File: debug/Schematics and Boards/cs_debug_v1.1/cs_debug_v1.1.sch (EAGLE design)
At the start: 217 parts, among them J1 J-JTAG-CORTEX_SMD, J19 Solar, J3 HIROSE-DF40_50-PIN_CONNECTORS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, J5 J-WURTH-USBC, Q10 2N7002P, Q3 FDN340P, Q4 2N7002P, Q5 FDN340P, Q6 2N7002P, Q7 FDN340P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

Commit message: DBG: change a few passive components for lower cost option.
Have NOT regenerated the BOM or CAM yet
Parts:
- R22, R23, R31, R32, R38, R39, R58: MPN ERJ-3BQF5R1V -> ERJ-U03F5R10V; PART_NO ERJ-3BQF5R1V -> ERJ-U03F5R10V
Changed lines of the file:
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@@
 </part>
 <part name="R58" library="Resistors" deviceset="R-" device="0603" value="5.1">
-<attribute name="MPN" value="ERJ-3BQF5R1V"/>
-<attribute name="PART_NO" value="ERJ-3BQF5R1V"/>
+<attribute name="MPN" value="ERJ-U03F5R10V"/>
+<attribute name="PART_NO" value="ERJ-U03F5R10V"/>
 <attribute name="TOL" value="1%"/>
 </part>
@@
 </part>
 <part name="R38" library="Resistors" deviceset="R-" device="0603" value="5.1">
-<attribute name="MPN" value="ERJ-3BQF5R1V"/>
-<attribute name="PART_NO" value="ERJ-3BQF5R1V"/>
+<attribute name="MPN" value="ERJ-U03F5R10V"/>
+<attribute name="PART_NO" value="ERJ-U03F5R10V"/>
 <attribute name="TOL" value="1%"/>
 </part>
@@
 <part name="U$29" library="SparkFun-PowerSymbols" deviceset="AGND" device=""/>
 <part name="R39" library="Resistors" deviceset="R-" device="0603" value="5.1">
-<attribute name="MPN" value="ERJ-3BQF5R1V"/>
-<attribute name="PART_NO" value="ERJ-3BQF5R1V"/>
+<attribute name="MPN" value="ERJ-U03F5R10V"/>
+<attribute name="PART_NO" value="ERJ-U03F5R10V"/>
 <attribute name="TOL" value="1%"/>
 </part>
@@
 </part>
 <part name="R31" library="Resistors" deviceset="R-" device="0603" value="5.1">
-<attribute name="MPN" value="ERJ-3BQF5R1V"/>
-<attribute name="PART_NO" value="ERJ-3BQF5R1V"/>
+<attribute name="MPN" value="ERJ-U03F5R10V"/>
+<attribute name="PART_NO" value="ERJ-U03F5R10V"/>
 <attribute name="TOL" value="1%"/>
 </part>
@@
 <part name="U$24" library="SparkFun-PowerSymbols" deviceset="AGND" device=""/>
 <part name="R32" library="Resistors" deviceset="R-" device="0603" value="5.1">
-<attribute name="MPN" value="ERJ-3BQF5R1V"/>
-<attribute name="PART_NO" value="ERJ-3BQF5R1V"/>
+<attribute name="MPN" value="ERJ-U03F5R10V"/>
+<attribute name="PART_NO" value="ERJ-U03F5R10V"/>
 <attribute name="TOL" value="1%"/>
 </part>
@@
 </part>
 <part name="R22" library="Resistors" deviceset="R-" device="0603" value="5.1">
-<attribute name="MPN" value="ERJ-3BQF5R1V"/>
-<attribute name="PART_NO" value="ERJ-3BQF5R1V"/>
+<attribute name="MPN" value="ERJ-U03F5R10V"/>
+<attribute name="PART_NO" value="ERJ-U03F5R10V"/>
 <attribute name="TOL" value="1%"/>
 </part>
@@
 <part name="U$17" library="SparkFun-PowerSymbols" deviceset="AGND" device=""/>
 <part name="R23" library="Resistors" deviceset="R-" device="0603" value="5.1">
-<attribute name="MPN" value="ERJ-3BQF5R1V"/>
-<attribute name="PART_NO" value="ERJ-3BQF5R1V"/>
-<attribute name="TOL" value="1%"/>
-</part>
+<attribute name="MPN" value="ERJ-U03F5R10V"/>
+<attribute name="PART_NO" value="ERJ-U03F5R10V"/>
+<attribute name="TOL" value="1%"/>
+</part>

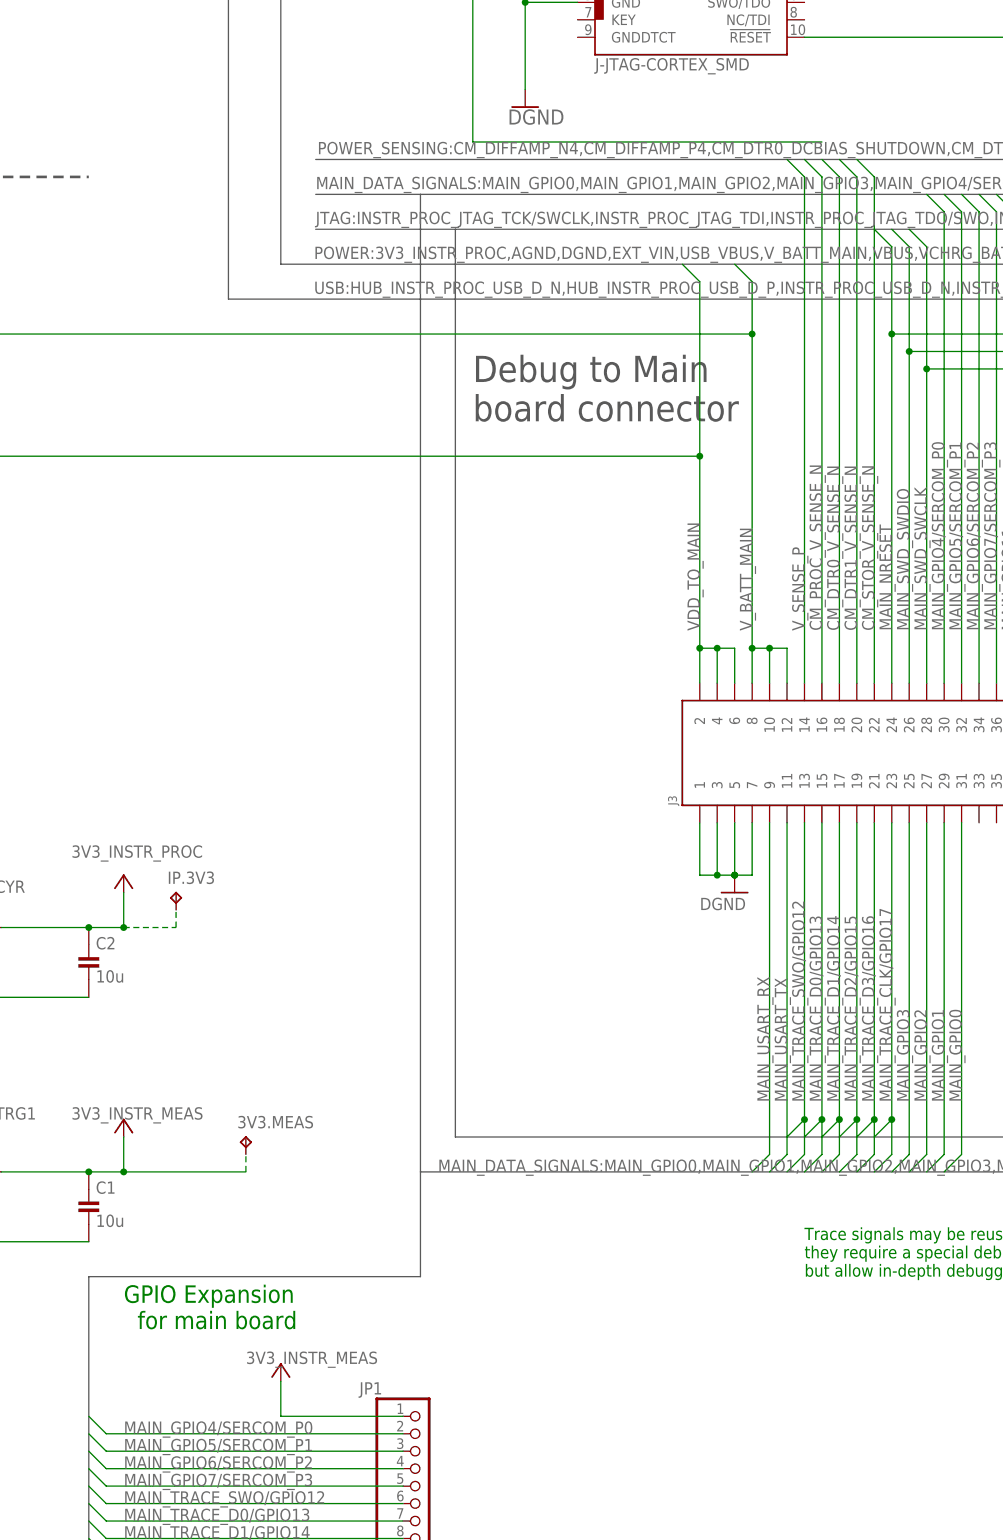
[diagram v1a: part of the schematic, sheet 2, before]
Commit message: Update files per design review and regenerate CAM
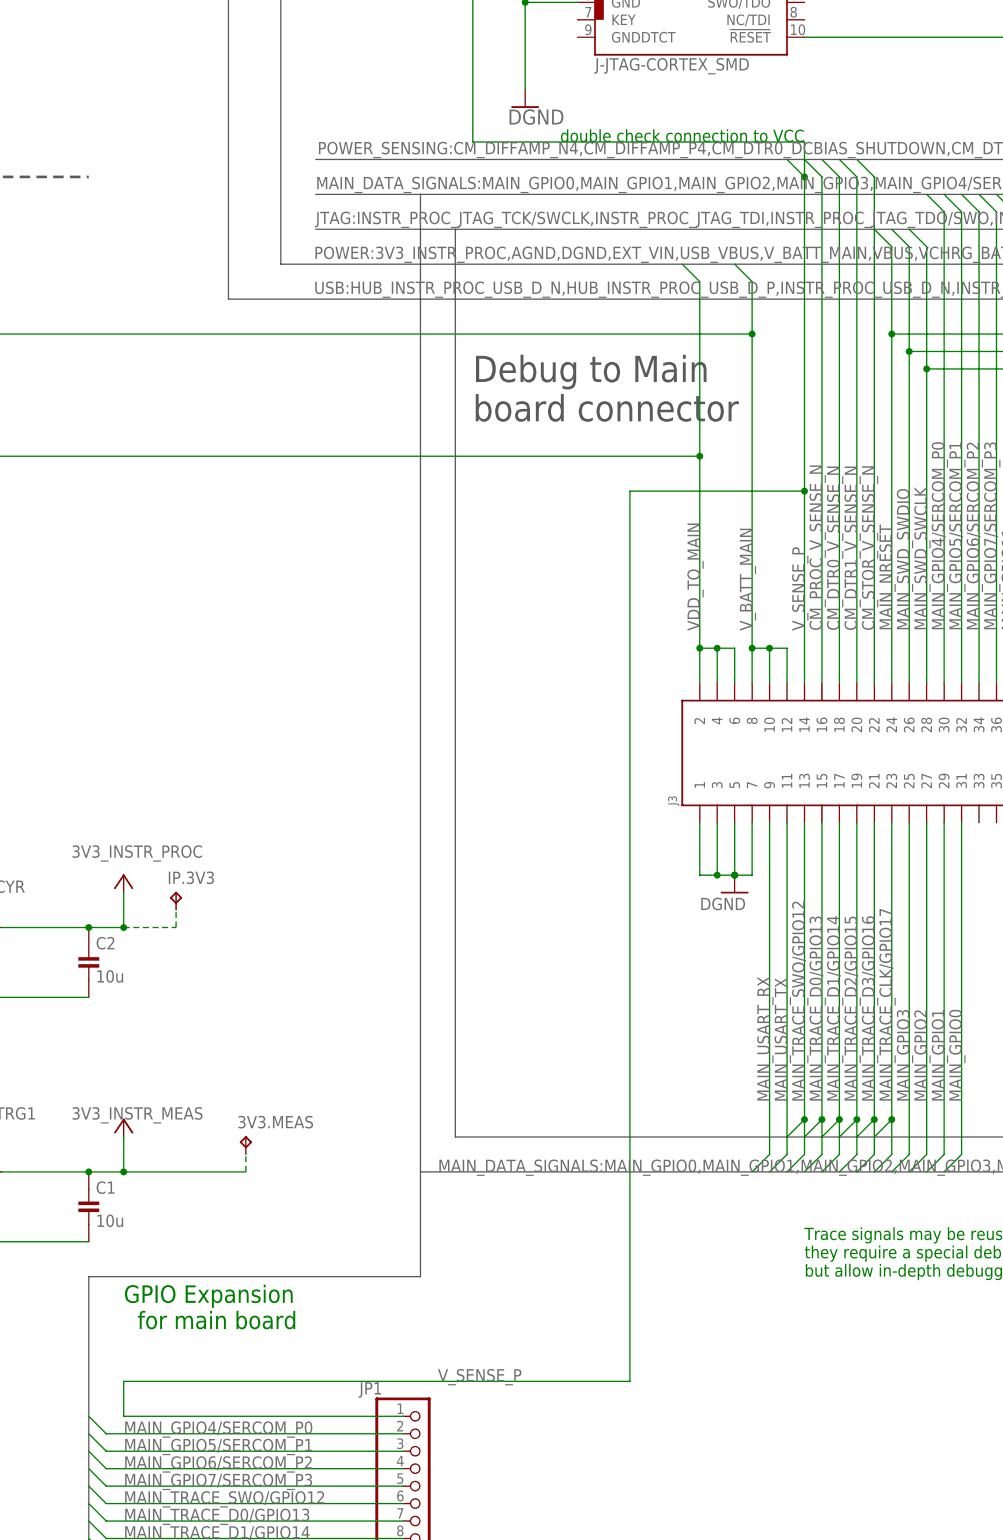
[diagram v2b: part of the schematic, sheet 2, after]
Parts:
- J5: MPN (none) -> 632723300011; PART_NO 632723100011 -> 632723300011
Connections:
- net 3V3_INSTR_MEAS: no longer JP1.1
- net V_SENSE_P: now also JP1.1
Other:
- note added: "double check connection to VCC"
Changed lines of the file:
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@@
 </part>
 <part name="J5" library="Connectors" deviceset="J-WURTH-USBC" device="">
-<attribute name="PART_NO" value="632723100011"/>
+<attribute name="MPN" value="632723300011"/>
+<attribute name="PART_NO" value="632723300011"/>
 </part>
 <part name="GND20" library="Supplies" deviceset="GND" device=""/>
@@
 <attribute name="PART_NO" value="TSW-112-07-T-S"/>
 </part>
-<part name="SUPPLY11" library="Supplies" deviceset="+3V3" device=""/>
 <part name="GND6" library="Supplies" deviceset="GND" device=""/>
 <part name="CHRG" library="Connectors" deviceset="JUMPER-SMT_2_NC_PASTE" device="_NO-SILK" package3d_urn="urn:adsk.eagle:package:39283/1"/>
@@
 <text x="203.2" y="172.72" size="1.778" layer="91">Mark port 2
   as removeable</text>
+<text x="457.2" y="226.06" size="1.778" layer="91">double check connection to VCC</text>
 </plain>
 <instances>
@@
 <attribute name="PART_NO" x="436.88" y="25.4" size="1.778" layer="96" display="off"/>
 </instance>
-<instance part="SUPPLY11" gate="G$1" x="416.56" y="48.26" smashed="yes"/>
 <instance part="GND6" gate="1" x="416.56" y="5.08" smashed="yes"/>
 <instance part="CHRG" gate="G$1" x="76.2" y="114.3" smashed="yes" rot="R90">
@@
 <net name="V_SENSE_P" class="0">
 <segment>
-<wire x1="495.3" y1="226.06" x2="444.5" y2="226.06" width="0.1524" layer="91"/>
+<pinref part="J3" gate="G$1" pin="14"/>
+<wire x1="492.76" y1="147.32" x2="492.76" y2="175.26" width="0.1524" layer="91"/>
+<label x="492.76" y="154.94" size="1.778" layer="95" rot="R90"/>
+<wire x1="492.76" y1="175.26" x2="492.76" y2="220.98" width="0.1524" layer="91"/>
+<wire x1="492.76" y1="220.98" x2="490.22" y2="223.52" width="0.1524" layer="91"/>
 <pinref part="J1" gate="G$1" pin="VCC"/>
+<wire x1="492.76" y1="226.06" x2="444.5" y2="226.06" width="0.1524" layer="91"/>
 <wire x1="444.5" y1="251.46" x2="459.74" y2="251.46" width="0.1524" layer="91"/>
 <wire x1="444.5" y1="251.46" x2="444.5" y2="226.06" width="0.1524" layer="91"/>
-</segment>
-<segment>
-<pinref part="J3" gate="G$1" pin="14"/>
-<wire x1="492.76" y1="147.32" x2="492.76" y2="220.98" width="0.1524" layer="91"/>
-<label x="492.76" y="154.94" size="1.778" layer="95" rot="R90"/>
-<wire x1="492.76" y1="220.98" x2="490.22" y2="223.52" width="0.1524" layer="91"/>
+<wire x1="492.76" y1="220.98" x2="492.76" y2="226.06" width="0.1524" layer="91"/>
+<junction x="492.76" y="220.98"/>
+<wire x1="492.76" y1="175.26" x2="467.36" y2="175.26" width="0.1524" layer="91"/>
+<wire x1="467.36" y1="175.26" x2="467.36" y2="45.72" width="0.1524" layer="91"/>
+<junction x="492.76" y="175.26"/>
+<wire x1="467.36" y1="45.72" x2="393.7" y2="45.72" width="0.1524" layer="91"/>
+<wire x1="393.7" y1="45.72" x2="393.7" y2="40.64" width="0.1524" layer="91"/>
+<pinref part="JP1" gate="G$1" pin="1"/>
+<wire x1="393.7" y1="40.64" x2="434.34" y2="40.64" width="0.1524" layer="91"/>
+<label x="439.42" y="45.72" size="1.778" layer="95"/>
 </segment>
 </net>
@@
 <junction x="393.7" y="76.2"/>
 </segment>
-<segment>
-<label x="411.48" y="48.26" size="1.778" layer="95"/>
-<pinref part="SUPPLY11" gate="G$1" pin="+3V3"/>
-<wire x1="416.56" y1="40.64" x2="416.56" y2="45.72" width="0.1524" layer="91"/>
-<pinref part="JP1" gate="G$1" pin="1"/>
-<wire x1="434.34" y1="40.64" x2="416.56" y2="40.64" width="0.1524" layer="91"/>
-</segment>
-</net>
+</net>

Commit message: Minor part renaming per octopart BOM tool
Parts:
- Q10, Q4, Q6, Q8: MPN (none) -> 2N7002P,215; PART_NO 2N7002P -> 2N7002P,215
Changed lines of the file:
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@@
 </part>
 <part name="Q10" library="Switches" deviceset="2N7002P" device="">
-<attribute name="PART_NO" value="2N7002P"/>
+<attribute name="MPN" value="2N7002P,215"/>
+<attribute name="PART_NO" value="2N7002P,215"/>
 </part>
 <part name="U$34" library="SparkFun-PowerSymbols" deviceset="AGND" device=""/>
@@
 </part>
 <part name="Q6" library="Switches" deviceset="2N7002P" device="">
-<attribute name="PART_NO" value="2N7002P"/>
+<attribute name="MPN" value="2N7002P,215"/>
+<attribute name="PART_NO" value="2N7002P,215"/>
 </part>
 <part name="U$28" library="SparkFun-PowerSymbols" deviceset="AGND" device=""/>
@@
 </part>
 <part name="Q8" library="Switches" deviceset="2N7002P" device="">
-<attribute name="PART_NO" value="2N7002P"/>
+<attribute name="MPN" value="2N7002P,215"/>
+<attribute name="PART_NO" value="2N7002P,215"/>
 </part>
 <part name="U$23" library="SparkFun-PowerSymbols" deviceset="AGND" device=""/>
@@
 </part>
 <part name="Q4" library="Switches" deviceset="2N7002P" device="">
-<attribute name="PART_NO" value="2N7002P"/>
+<attribute name="MPN" value="2N7002P,215"/>
+<attribute name="PART_NO" value="2N7002P,215"/>
 </part>
 <part name="U$16" library="SparkFun-PowerSymbols" deviceset="AGND" device=""/>
